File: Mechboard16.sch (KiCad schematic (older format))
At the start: 153 parts, among them CN1 CONN_C16, CN2 CONN_+4, SW0:0 KEY_DEL, SW0:1 KEY_RET, SW0:2 KEY_PND, SW0:3 KEY_HLP, SW0:4 KEY_F1, SW0:5 KEY_F2, SW0:6 KEY_F3, SW0:7 KEY_AT, SW1:0 KEY_3, SW1:1 KEY_W, SW1:2 KEY_A, SW1:3 KEY_4, SW1:4 KEY_Z, SW1:5 KEY_S, SW1:6 KEY_E, SW1:7 KEY_LSH, SW1B:7 KEY_RSH, SW1C:7 KEY_CLK, SW2:0 KEY_5, SW2:1 KEY_R, SW2:2 KEY_D, SW2:3 KEY_6, SW2:4 KEY_C, SW2:5 KEY_F, SW2:6 KEY_T, SW2:7 KEY_X, SW3:0 KEY_7, SW3:1 KEY_Y, SW3:2 KEY_G, SW3:3 KEY_8, SW3:4 KEY_B, SW3:5 KEY_H, SW3:6 KEY_U, SW3:7 KEY_V, SW4:0 KEY_9, SW4:1 KEY_I, SW4:2 KEY_J, SW4:3 KEY_0, SW4:4 KEY_M, SW4:5 KEY_K, SW4:6 KEY_O, SW4:7 KEY_N, SW5:0 KEY_DN, SW5:1 KEY_P, SW5:2 KEY_L, SW5:3 KEY_UP, SW5:4 KEY_DOT, SW5:5 KEY_COL, SW5:6 KEY_MIN, SW5:7 KEY_COM, SW6:0 KEY_LF, SW6:1 KEY_AST, SW6:2 KEY_SEM, SW6:3 KEY_RT, SW6:4 KEY_ESC, SW6:5 KEY_EQ, SW6:6 KEY_PLS, SW6:7 KEY_SLA, SW7:0 KEY_1, SW7:1 KEY_CLR, SW7:2 KEY_CTL, SW7:3 KEY_2, SW7:4 KEY_SPC, SW7:5 KEY_CMD, SW7:6 KEY_Q, SW7:7 KEY_RUN, U1 4066, U2 NE555, U3 RP2040_Zero

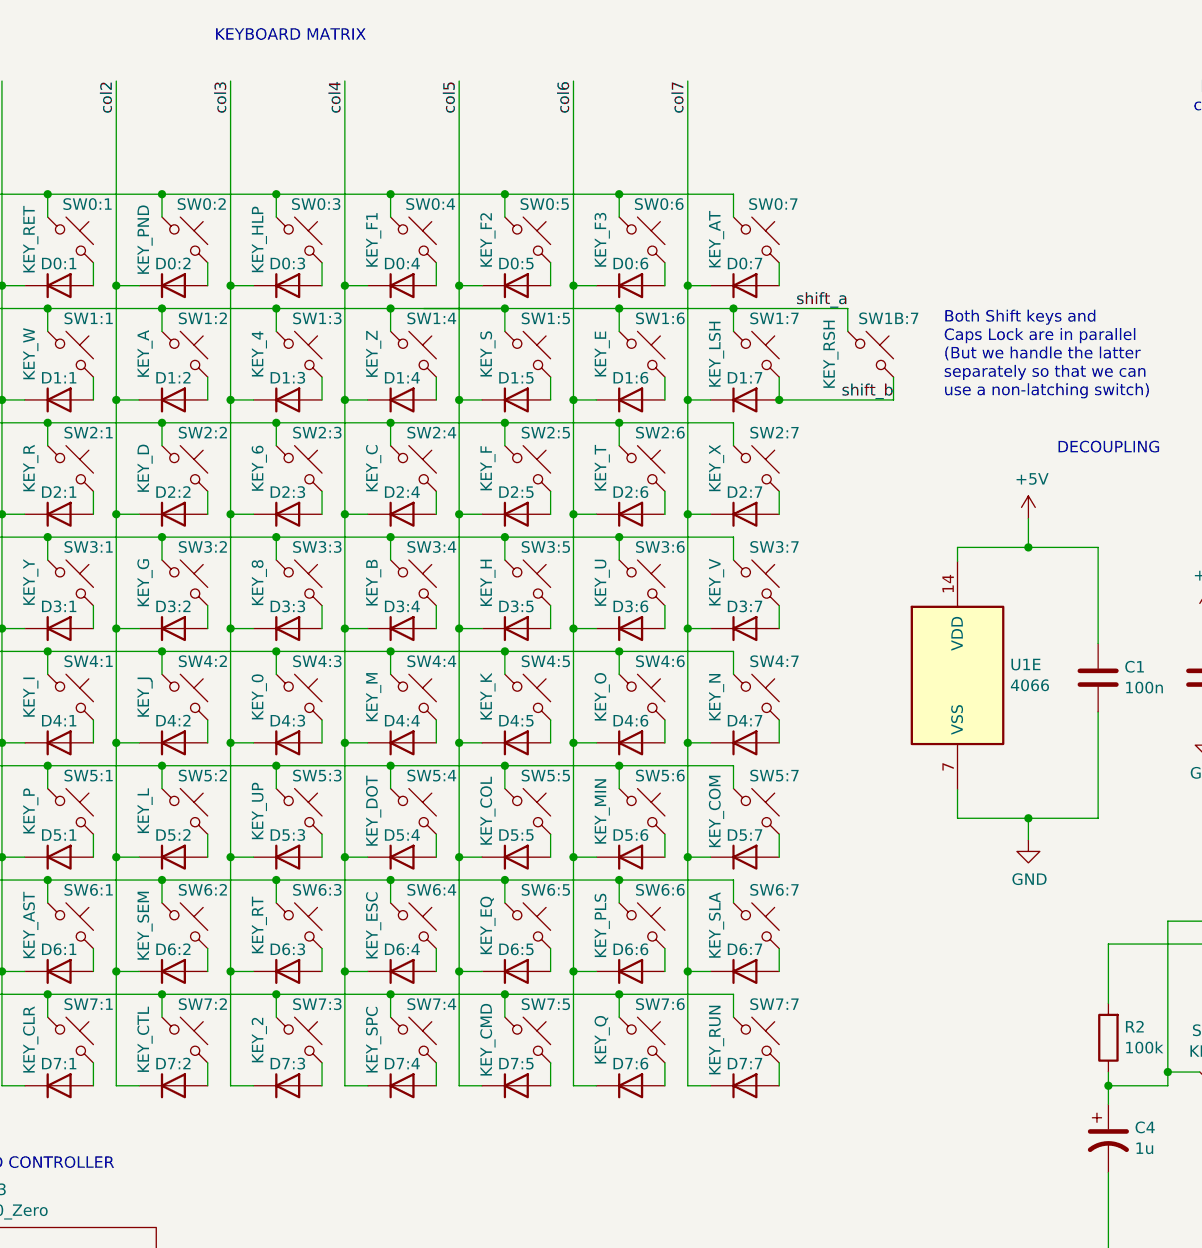
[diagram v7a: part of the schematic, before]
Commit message: Better alignment of R3 and start adding centered footprints for 1.5U keys
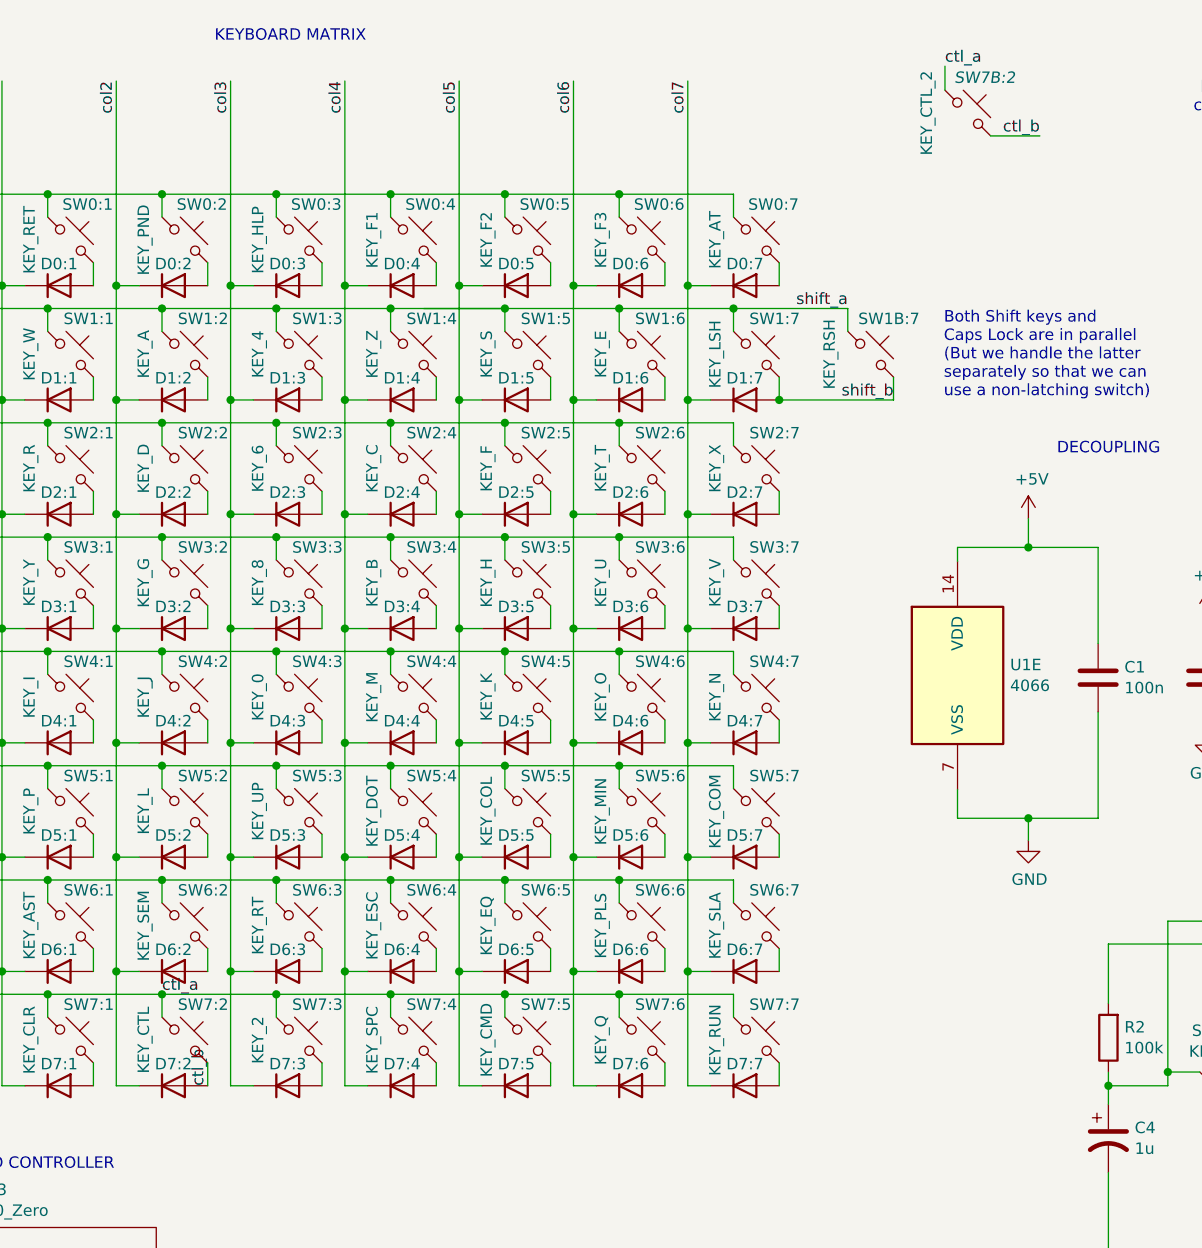
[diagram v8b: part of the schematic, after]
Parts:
- added SW7B:2: KEY_CTL_2, Mechboard16:SW_Cherry_MX_PCB_1.50u, symbol Switch:SW_Push_45deg
- SW7:1: footprint Mechboard16:SW_Cherry_MX_PCB_1.50u -> Mechboard16:SW_Cherry_MX_PCB_1.00u
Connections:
- net ctl_b: now reaches D7:2.2 (A), SW7:2.2
- net ctl_b: now also SW7B:2.2
- net row7 renamed ctl_a
- net ctl_a: now also SW7B:2.1
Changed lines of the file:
@@
 F 0 "SW7:1" H 2355 5190 50  0000 C CNN
 F 1 "KEY_CLR" V 2095 5035 50  0000 C CNN
-F 2 "Mechboard16:SW_Cherry_MX_PCB_1.50u" H 2275 5035 50  0001 C CNN
+F 2 "Mechboard16:SW_Cherry_MX_PCB_1.00u" H 2275 5035 50  0001 C CNN
 F 3 "~" H 2275 5035 50  0001 C CNN
 	1    2275 5035
@@
 	1    0    0    -1
 $EndComp
+$Comp
+L Switch:SW_Push_45deg SW7B:2
+U 1 1 6971412A
+P 6200 980
+F 0 "SW7B:2" H 6275 1135 50  0000 C CIN
+F 1 "KEY_CTL_2" V 6020 980 50  0000 C CNN
+F 2 "Mechboard16:SW_Cherry_MX_PCB_1.50u" H 6200 980 50  0001 C CNN
+F 3 "~" H 6200 980 50  0001 C CNN
+	1    6200 980
+	1    0    0    -1
+$EndComp
+Wire Wire Line
+	6100 880  6100 775
+Text Label 6100 775  0    50   ~ 0
+ctl_a
+Text Label 2675 4835 0    50   ~ 0
+ctl_a
+Text Label 2875 5235 1    50   ~ 0
+ctl_b
+Text Label 6515 1080 2    50   ~ 0
+ctl_b
+Wire Wire Line
+	6300 1080 6515 1080
 $EndSCHEMATC
